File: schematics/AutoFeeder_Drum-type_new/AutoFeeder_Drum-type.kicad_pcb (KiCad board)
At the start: 2 copper layers, 68.5 x 80 mm, 60 parts, among them J1 USB_C_Receptacle_6, J2 Conn_01x04, J3 Conn_01x05, J4 Conn_02x02_Odd_Even, J5 Conn_01x04, J6 Conn_02x03_Odd_Even, J7 Conn_01x04, J8 Conn_01x03, J9 Conn_01x04, M1 Motor_DC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

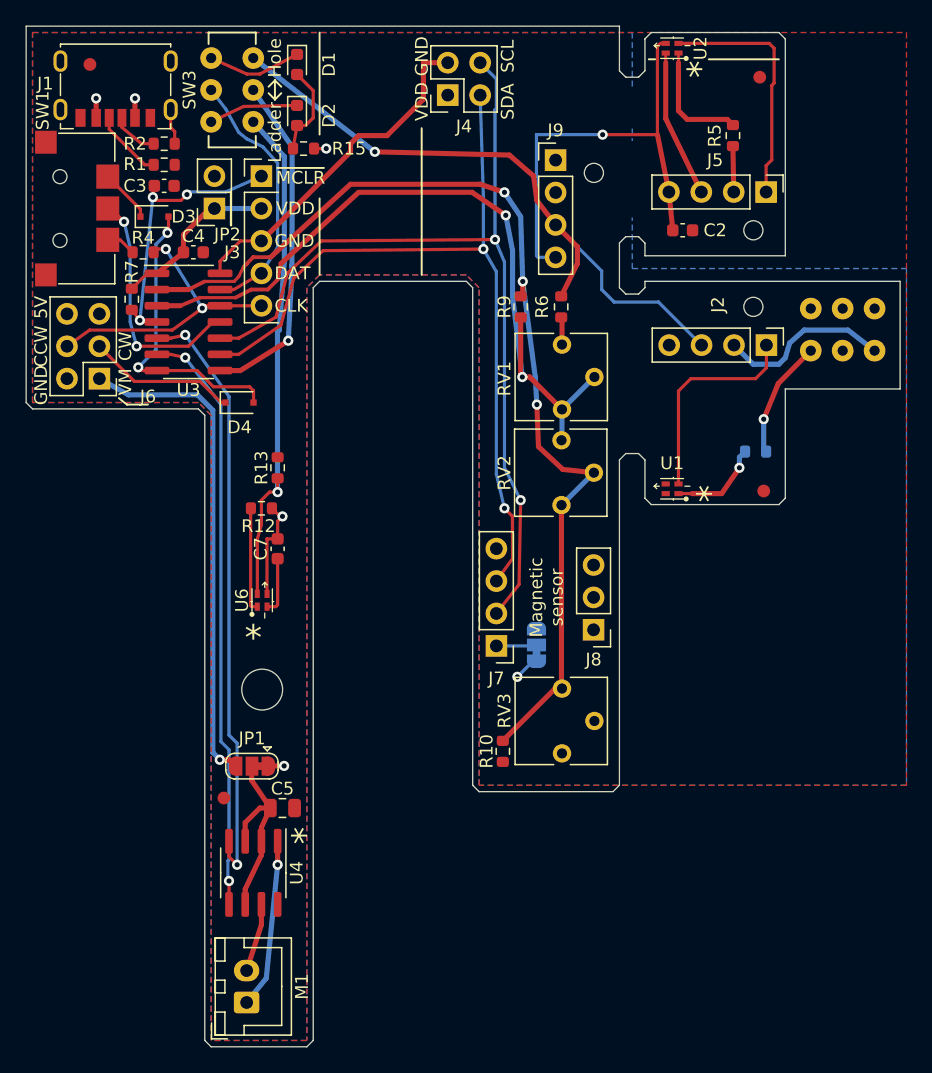
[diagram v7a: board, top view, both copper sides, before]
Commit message: Change the position of M3 mounting hole / Add silk printing of magnetic sensor / Add Diode OR (D3,D4) to allow advancing one component either by manual switch or automatic control / Slightly modified pattern routing. Completed as Rev.02 board
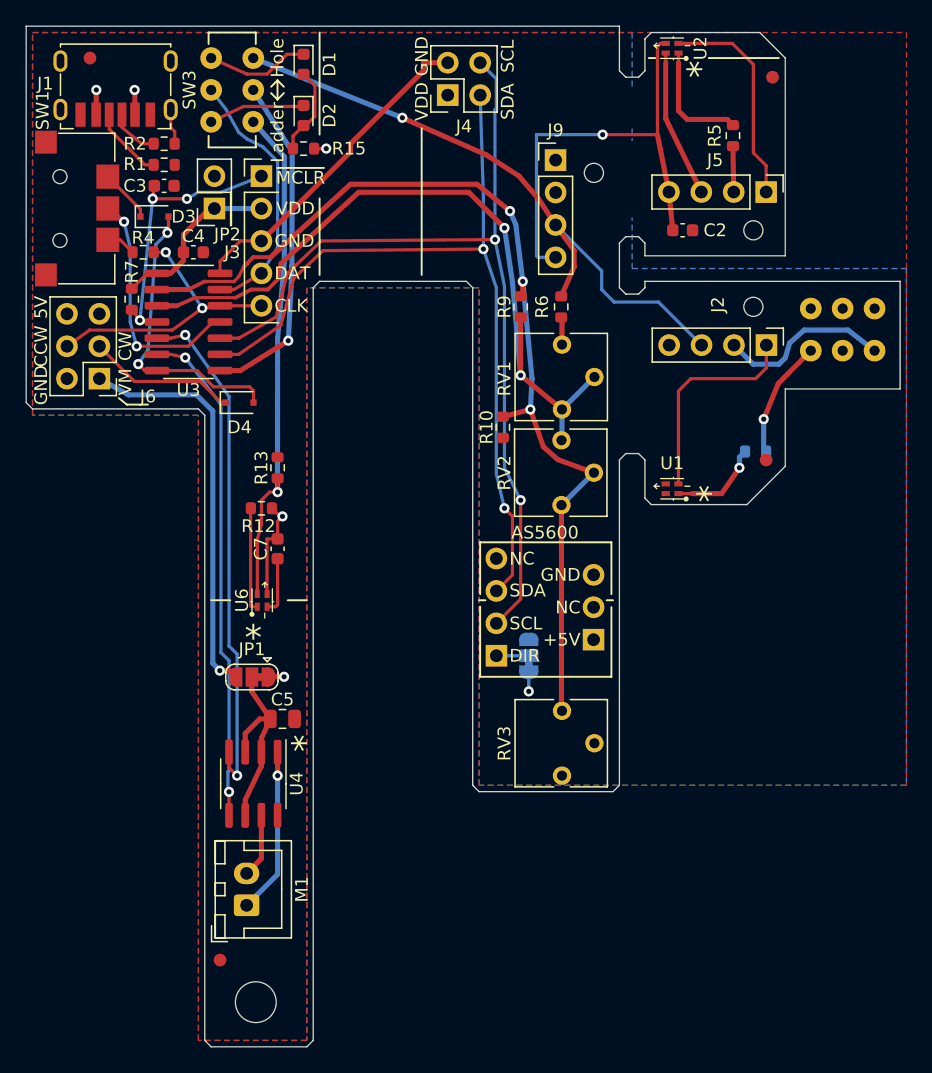
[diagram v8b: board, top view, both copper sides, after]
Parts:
- moved R10 25.4 mm to (173.9, 91.4)
- moved REF** 24.5 mm to (154.5, 136.5)
- moved REF** 12.7 mm to (151.7, 133.2)
- moved M1 7.62 mm to (153.8, 128.9)
- moved C5 6.98 mm to (156.6, 114.3)
- moved JP1 6.98 mm to (154.2, 111.0)
- moved U4 6.98 mm to (154.3, 119.4)
- moved ? 2.44 mm to (194.5, 94.0)
- moved RV3 1.75 mm to (178.5, 118.7)
- moved JP3 1.04 mm to (175.9, 109.3)
- moved ? 1.00 mm to (195.0, 64.0)
- moved J8 0.77 mm to (181.0, 108.1)
- moved J7 0.77 mm to (173.4, 109.3)
- moved D1 0.51 mm to (158.2, 63.0)
- moved D2 0.51 mm to (158.2, 67.0)
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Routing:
- net Net-(J6-Pad1): track 38.8 -> 31.7 mm
- net /REV: track 46.4 -> 39.4 mm
- net /FWD: track 47.2 -> 40.3 mm
- net GND: track 72.5 -> 68.5 mm
- net /RA5: track 81.6 -> 78.3 mm
- net /Sensor0: track 52.2 -> 50.1 mm
- net +5V: track 49.4 -> 50.7 mm
- net /SCL: track 70.5 -> 71.3 mm
- net /RA4: track 59.4 -> 58.6 mm
- net /SDA: track 64.1 -> 64.9 mm
- net Net-(D1-Pad1): track 7.38 -> 8.15 mm
- net Net-(J7-Pad1): track 3.18 -> 2.54 mm
- net Net-(D2-Pad1): track 7.01 -> 7.55 mm
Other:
- outline, holes or cut-outs redrawn
- board text added: "AS5600"
- board text added: "DIR"
- board text added: "NC"
- board text added: "Rev.02 * Add Fiducals * Add holes, labels, etc. * Increase the length of Type-C pins"
- board text removed: "Magnetic sensor"
- board text removed: "Rev.02 * Add Fiducals * Add holes, labels, etc."
